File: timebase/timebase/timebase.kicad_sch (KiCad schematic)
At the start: 59 parts, among them J402 Jack-DC, J404 Jack-DC, J8 Conn_Coaxial, J9 Conn_Coaxial

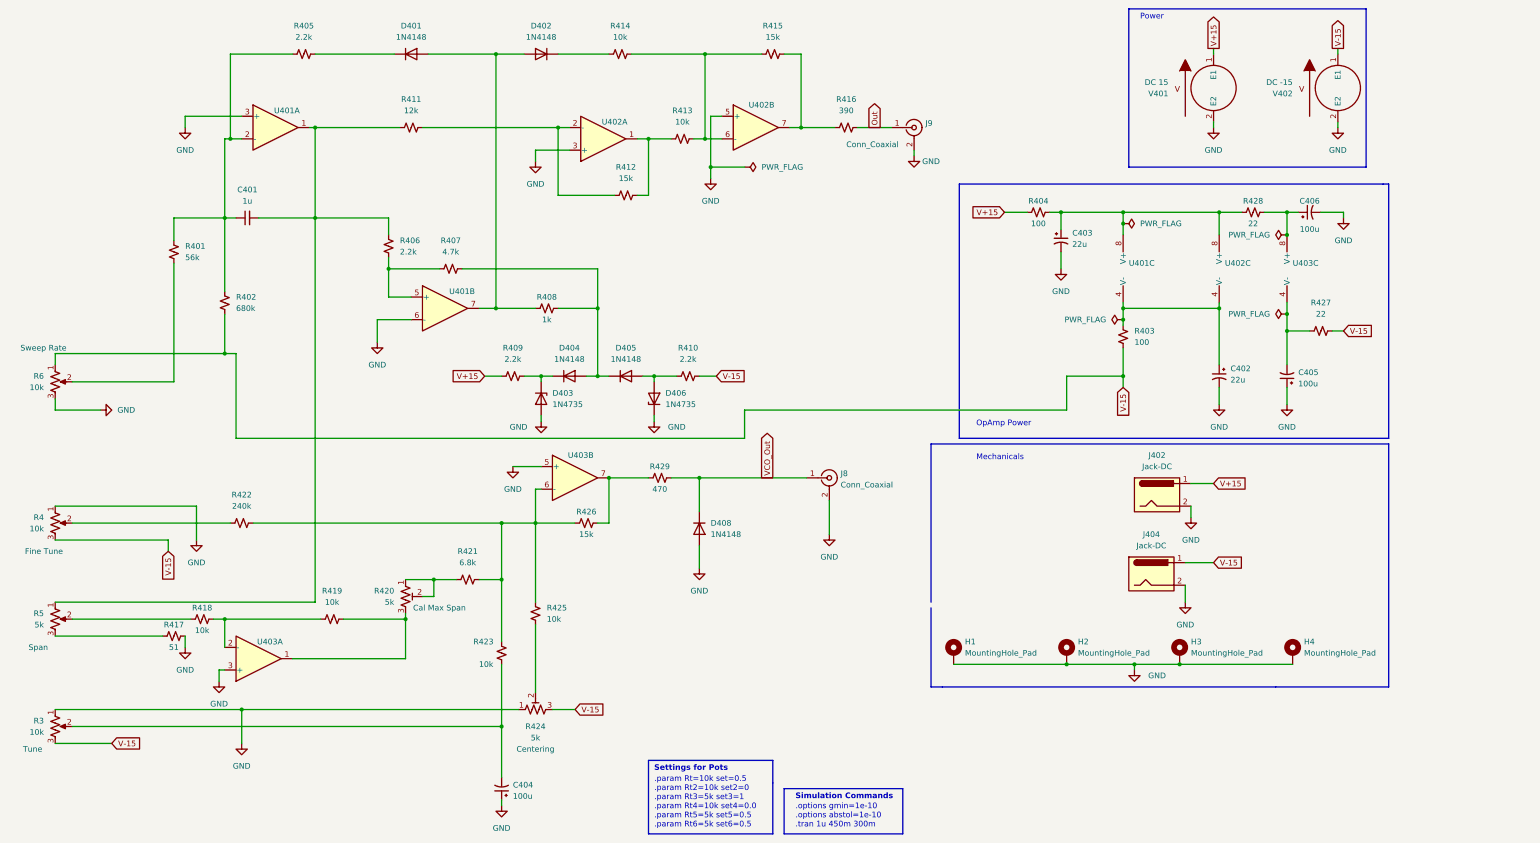
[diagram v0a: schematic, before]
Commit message: Changes to 15v supply including symbol annotation, BOM, footprints, and folder reorg
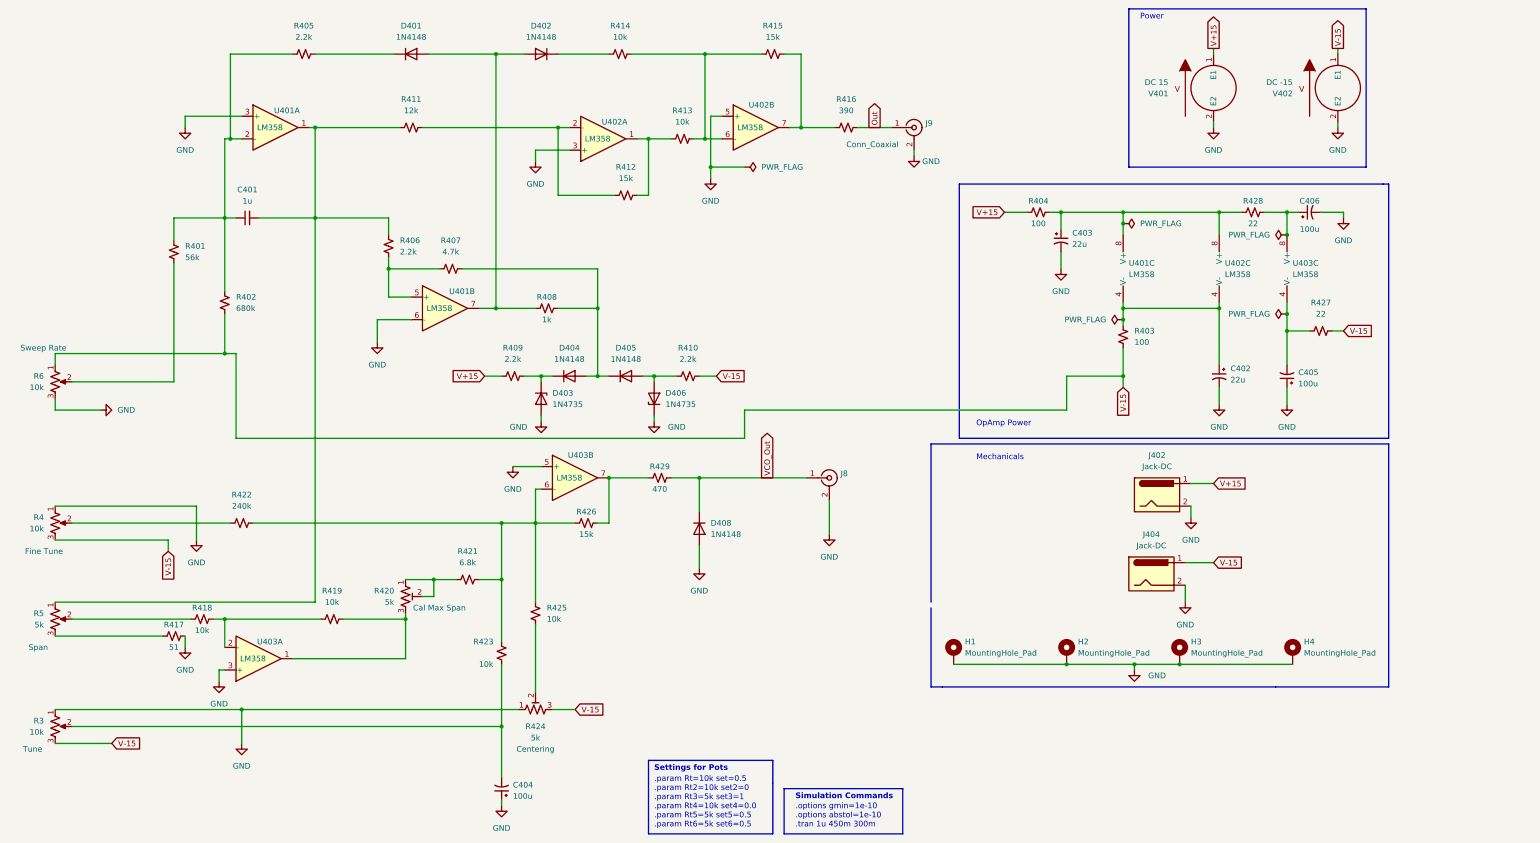
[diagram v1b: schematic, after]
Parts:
- J8: value Conn_Coaxial -> (none); footprint SnapEDA Library:TE_5-1634503-1 -> (none)
- U401, U402, U403: value (none) -> LM358; footprint (none) -> SnapEDA Library:DIP794W45P254L959H508Q8
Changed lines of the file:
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@@
     (in_bom yes) (on_board yes)
     (property "Reference" "U403" (id 0) (at 80.01 158.75 0))
-    (property "Value" "" (id 1) (at 76.2 162.56 0))
-    (property "Footprint" "" (id 2) (at 77.47 162.56 0)
+    (property "Value" "LM358" (id 1) (at 76.2 162.56 0))
+    (property "Footprint" "SnapEDA Library:DIP794W45P254L959H508Q8" (id 2) (at 77.47 162.56 0)
       (effects (font (size 1.27 1.27)) hide)
     )
@@
       (effects (font (size 1.27 1.27)) (justify left))
     )
-    (property "Value" "" (id 1) (at 273.05 76.1999 0)
-      (effects (font (size 1.27 1.27)) (justify left))
-    )
-    (property "Footprint" "" (id 2) (at 274.32 74.93 0)
+    (property "Value" "LM358" (id 1) (at 273.05 76.1999 0)
+      (effects (font (size 1.27 1.27)) (justify left))
+    )
+    (property "Footprint" "SnapEDA Library:DIP794W45P254L959H508Q8" (id 2) (at 274.32 74.93 0)
       (effects (font (size 1.27 1.27)) hide)
     )
@@
     (in_bom yes) (on_board yes)
     (property "Reference" "U402" (id 0) (at 157.48 41.91 0))
-    (property "Value" "" (id 1) (at 153.67 45.72 0))
-    (property "Footprint" "" (id 2) (at 154.94 45.72 0)
+    (property "Value" "LM358" (id 1) (at 153.67 45.72 0))
+    (property "Footprint" "SnapEDA Library:DIP794W45P254L959H508Q8" (id 2) (at 154.94 45.72 0)
       (effects (font (size 1.27 1.27)) hide)
     )
@@
       (effects (font (size 1.27 1.27)) (justify left))
     )
-    (property "Value" "Conn_Coaxial" (id 1) (at 208.28 123.4831 0)
-      (effects (font (size 1.27 1.27)) (justify left))
-    )
-    (property "Footprint" "SnapEDA Library:TE_5-1634503-1" (id 2) (at 205.74 121.92 0)
-      (effects (font (size 1.27 1.27)) hide)
-    )
-    (property "Datasheet" " ~" (id 3) (at 205.74 121.92 0)
+    (property "Value" "" (id 1) (at 208.28 123.4831 0)
+      (effects (font (size 1.27 1.27)) (justify left))
+    )
+    (property "Footprint" "" (id 2) (at 205.74 121.92 0)
+      (effects (font (size 1.27 1.27)) hide)
+    )
+    (property "Datasheet" "https://www.te.com/commerce/DocumentDelivery/DDEController?Action=srchrtrv&DocNm=1634503&DocType=Customer+Drawing&DocLang=English" (id 3) (at 205.74 121.92 0)
       (effects (font (size 1.27 1.27)) hide)
     )
@@
       (effects (font (size 1.27 1.27)) (justify left))
     )
-    (property "Value" "" (id 1) (at 309.88 76.1999 0)
-      (effects (font (size 1.27 1.27)) (justify left))
-    )
-    (property "Footprint" "" (id 2) (at 311.15 74.93 0)
+    (property "Value" "LM358" (id 1) (at 309.88 76.1999 0)
+      (effects (font (size 1.27 1.27)) (justify left))
+    )
+    (property "Footprint" "SnapEDA Library:DIP794W45P254L959H508Q8" (id 2) (at 311.15 74.93 0)
       (effects (font (size 1.27 1.27)) hide)
     )
@@
     (in_bom yes) (on_board yes)
     (property "Reference" "U403" (id 0) (at 149.86 116.84 0))
-    (property "Value" "" (id 1) (at 147.32 121.92 0))
-    (property "Footprint" "" (id 2) (at 148.59 121.92 0)
+    (property "Value" "LM358" (id 1) (at 147.32 121.92 0))
+    (property "Footprint" "SnapEDA Library:DIP794W45P254L959H508Q8" (id 2) (at 148.59 121.92 0)
       (effects (font (size 1.27 1.27)) hide)
     )
@@
       (effects (font (size 1.27 1.27)) (justify left))
     )
-    (property "Value" "" (id 1) (at 294.64 76.1999 0)
-      (effects (font (size 1.27 1.27)) (justify left))
-    )
-    (property "Footprint" "" (id 2) (at 295.91 74.93 0)
+    (property "Value" "LM358" (id 1) (at 294.64 76.1999 0)
+      (effects (font (size 1.27 1.27)) (justify left))
+    )
+    (property "Footprint" "SnapEDA Library:DIP794W45P254L959H508Q8" (id 2) (at 295.91 74.93 0)
       (effects (font (size 1.27 1.27)) hide)
     )
@@
     (in_bom yes) (on_board yes)
     (property "Reference" "U402" (id 0) (at 190.5 38.1 0))
-    (property "Value" "" (id 1) (at 187.96 43.18 0))
-    (property "Footprint" "" (id 2) (at 189.23 43.18 0)
+    (property "Value" "LM358" (id 1) (at 187.96 43.18 0))
+    (property "Footprint" "SnapEDA Library:DIP794W45P254L959H508Q8" (id 2) (at 189.23 43.18 0)
       (effects (font (size 1.27 1.27)) hide)
     )
@@
     (in_bom yes) (on_board yes)
     (property "Reference" "U401" (id 0) (at 123.19 80.01 0))
-    (property "Value" "" (id 1) (at 118.11 83.82 0))
-    (property "Footprint" "" (id 2) (at 119.38 83.82 0)
+    (property "Value" "LM358" (id 1) (at 118.11 83.82 0))
+    (property "Footprint" "SnapEDA Library:DIP794W45P254L959H508Q8" (id 2) (at 119.38 83.82 0)
       (effects (font (size 1.27 1.27)) hide)
     )
@@
     (in_bom yes) (on_board yes)
     (property "Reference" "U401" (id 0) (at 83.82 39.37 0))
-    (property "Value" "" (id 1) (at 80.01 43.18 0))
-    (property "Footprint" "" (id 2) (at 81.28 43.18 0)
-      (effects (font (size 1.27 1.27)) hide)
-    )
+    (property "Value" "LM358" (id 1) (at 80.01 43.18 0))
+    (property "Footprint" "SnapEDA Library:DIP794W45P254L959H508Q8" (id 2) (at 81.28 43.18 0)
+      (effects (font (size 1.27 1.27)) hide)
+    )

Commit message: if and log amp routing and 3d model
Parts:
- D401, D402, D404, D405, D408: Spice_Lib_File 1N4148.mod -> timebase-spice\1N4148.mod
- D403, D406: Spice_Lib_File 1N4735A.lib -> timebase-spice\1N4735A.lib
- J402, J404: footprint SnapEDA Library:CUI_PJ-007 -> timebase:CUI_PJ-007
- J8: value (none) -> Conn_Coaxial; footprint (none) -> timebase:TE_5-1634503-1
- J9: footprint SnapEDA Library:TE_5-1634503-1 -> timebase:TE_5-1634503-1
- R3: Spice_Lib_File Pot4.lib -> timebase-spice\Pot4.lib
- R4: Spice_Lib_File Pot2.lib -> timebase-spice\Pot2.lib
- R420: Spice_Lib_File Pot6.lib -> timebase-spice\Pot6.lib
- R424: Spice_Lib_File Pot5.lib -> timebase-spice\Pot5.lib
- R5: Spice_Lib_File Pot3.lib -> timebase-spice\Pot3.lib
- R6: Spice_Lib_File Pot.lib -> timebase-spice\Pot.lib
- U401, U402, U403: footprint SnapEDA Library:DIP794W45P254L959H508Q8 -> timebase:DIP794W45P254L959H508Q8; Spice_Lib_File LM358-dual.lib -> timebase-spice\LM358-dual.lib
- V401, V402: footprint SnapEDA Library:CUI_PJ-009A -> timebase:CUI_PJ-009A; now left out of the parts list

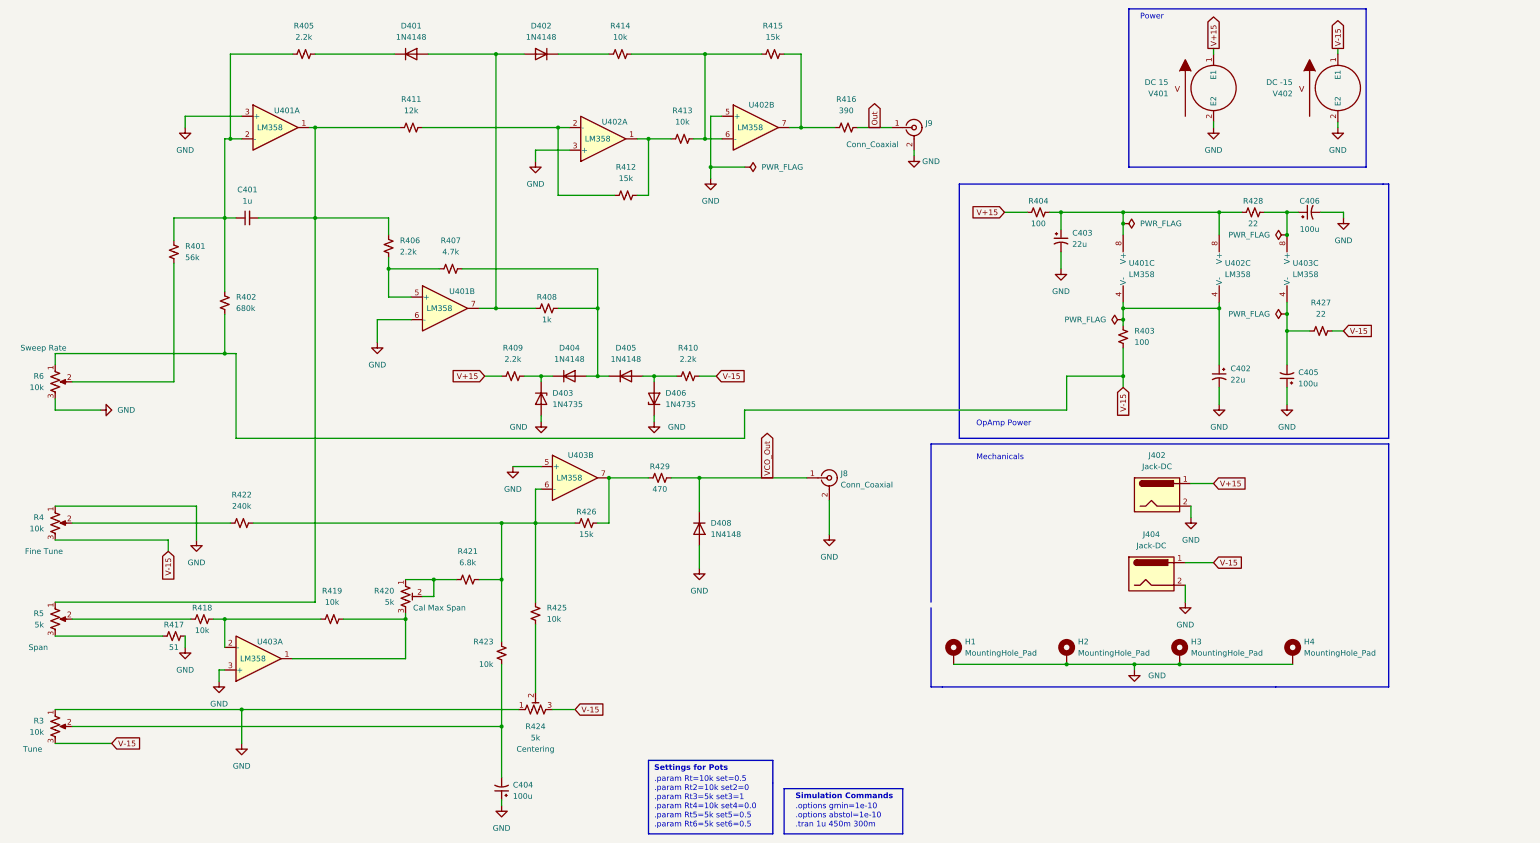
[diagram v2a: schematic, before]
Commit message: Improvements to if and log amp
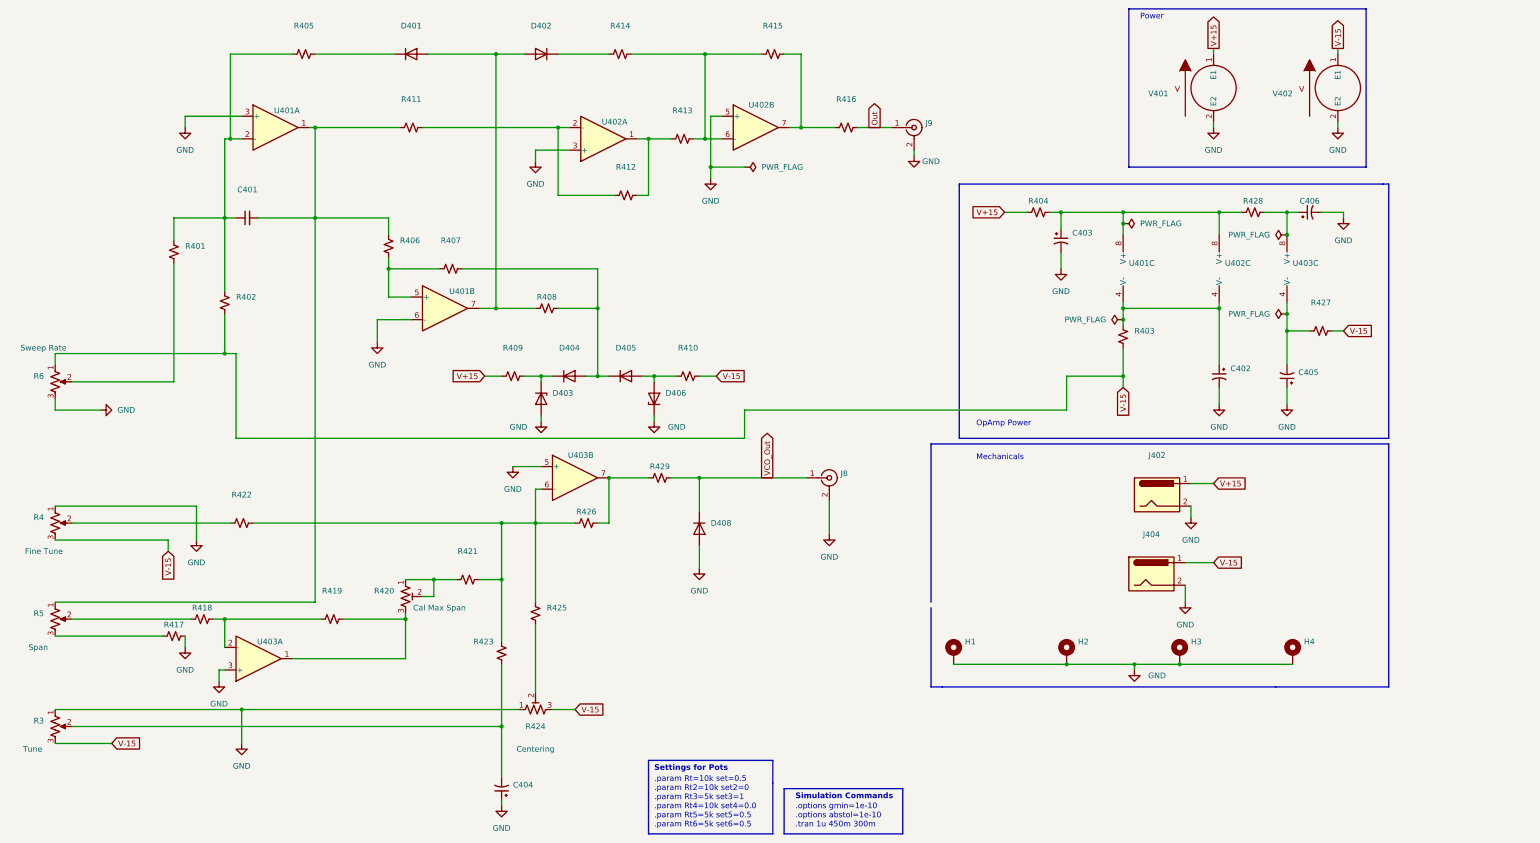
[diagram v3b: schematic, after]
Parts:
- C401: value 1u -> (none); footprint Capacitor_THT:C_Radial_D4.0mm_H5.0mm_P1.50mm -> (none)
- C402, C403: value 22u -> (none); footprint Capacitor_THT:CP_Axial_L11.0mm_D6.0mm_P18.00mm_Horizontal -> (none)
- C404, C405, C406: value 100u -> (none); footprint Capacitor_THT:CP_Axial_L11.0mm_D6.0mm_P18.00mm_Horizontal -> (none)
- D401, D402, D404, D405, D408: value 1N4148 -> (none); footprint Diode_THT:D_DO-35_SOD27_P7.62mm_Horizontal -> (none)
- D403, D406: value 1N4735 -> (none); footprint Diode_THT:D_DO-35_SOD27_P7.62mm_Horizontal -> (none)
- H1, H2, H3, H4: value MountingHole_Pad -> (none); footprint MountingHole:MountingHole_2.7mm_M2.5_DIN965_Pad_TopOnly -> (none)
- J402, J404: value Jack-DC -> (none); footprint timebase:CUI_PJ-007 -> (none)
- J8, J9: value Conn_Coaxial -> (none); footprint timebase:TE_5-1634503-1 -> (none)
- R3, R4, R6: value 10k -> (none); footprint Connector_Wire:SolderWire-0.127sqmm_1x03_P3.7mm_D0.48mm_OD1mm -> (none)
- R401: value 56k -> (none); footprint Resistor_THT:R_Axial_DIN0207_L6.3mm_D2.5mm_P7.62mm_Horizontal -> (none)
- R402: value 680k -> (none); footprint Resistor_THT:R_Axial_DIN0207_L6.3mm_D2.5mm_P7.62mm_Horizontal -> (none)
- R403, R404: value 100 -> (none); footprint Resistor_THT:R_Axial_DIN0207_L6.3mm_D2.5mm_P7.62mm_Horizontal -> (none)
- R405, R406, R409, R410: value 2.2k -> (none); footprint Resistor_THT:R_Axial_DIN0207_L6.3mm_D2.5mm_P7.62mm_Horizontal -> (none)
- R407: value 4.7k -> (none); footprint Resistor_THT:R_Axial_DIN0207_L6.3mm_D2.5mm_P7.62mm_Horizontal -> (none)
- R408: value 1k -> (none); footprint Resistor_THT:R_Axial_DIN0207_L6.3mm_D2.5mm_P7.62mm_Horizontal -> (none)
- R411: value 12k -> (none); footprint Resistor_THT:R_Axial_DIN0207_L6.3mm_D2.5mm_P7.62mm_Horizontal -> (none)
- R412, R415, R426: value 15k -> (none); footprint Resistor_THT:R_Axial_DIN0207_L6.3mm_D2.5mm_P7.62mm_Horizontal -> (none)
- R413, R414, R418, R419, R423, R425: value 10k -> (none); footprint Resistor_THT:R_Axial_DIN0207_L6.3mm_D2.5mm_P7.62mm_Horizontal -> (none)
- R416: value 390 -> (none); footprint Resistor_THT:R_Axial_DIN0207_L6.3mm_D2.5mm_P7.62mm_Horizontal -> (none)
- R417: value 51 -> (none); footprint Resistor_THT:R_Axial_DIN0207_L6.3mm_D2.5mm_P7.62mm_Horizontal -> (none)
- R420, R424: value 5k -> (none); footprint Potentiometer_THT:Potentiometer_Bourns_3296W_Vertical -> (none)
- R421: value 6.8k -> (none); footprint Resistor_THT:R_Axial_DIN0207_L6.3mm_D2.5mm_P7.62mm_Horizontal -> (none)
- R422: value 240k -> (none); footprint Resistor_THT:R_Axial_DIN0207_L6.3mm_D2.5mm_P7.62mm_Horizontal -> (none)
- R427, R428: value 22 -> (none); footprint Resistor_THT:R_Axial_DIN0207_L6.3mm_D2.5mm_P7.62mm_Horizontal -> (none)
- R429: value 470 -> (none); footprint Resistor_THT:R_Axial_DIN0207_L6.3mm_D2.5mm_P7.62mm_Horizontal -> (none)
- R5: value 5k -> (none); footprint Connector_Wire:SolderWire-0.127sqmm_1x03_P3.7mm_D0.48mm_OD1mm -> (none)
- U401, U402, U403: value LM358 -> (none); footprint timebase:DIP794W45P254L959H508Q8 -> (none)
- V401: value DC 15 -> (none); footprint timebase:CUI_PJ-009A -> (none)
- V402: value DC -15 -> (none); footprint timebase:CUI_PJ-009A -> (none)
